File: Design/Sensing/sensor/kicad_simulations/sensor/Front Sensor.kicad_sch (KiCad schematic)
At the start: 9 parts, among them Q1 2N3904, U1 TSSP58038

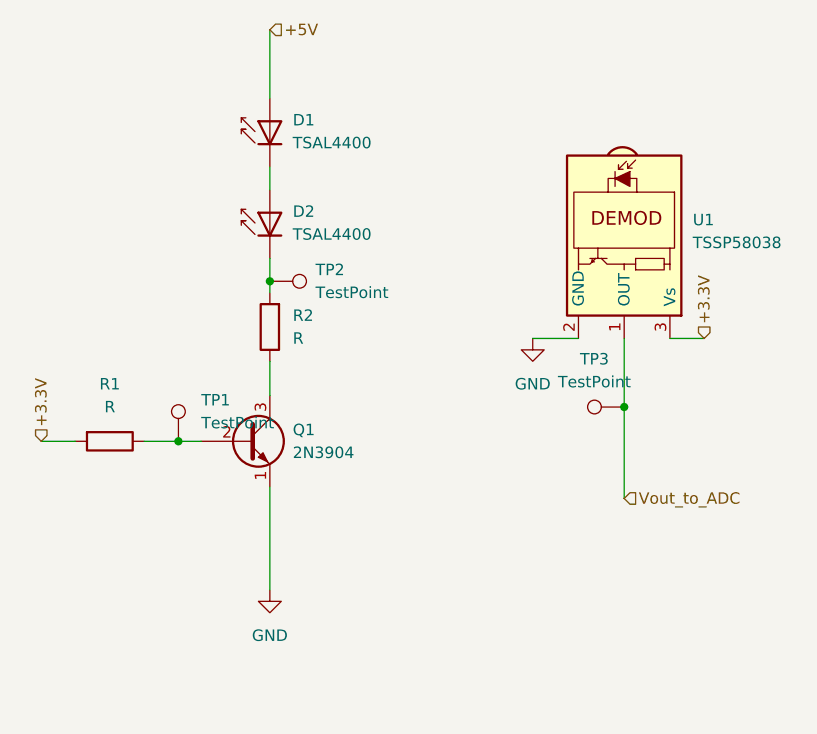
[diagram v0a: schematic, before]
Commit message: Resistor values for emitter circuit done, still have to name the circuits properly
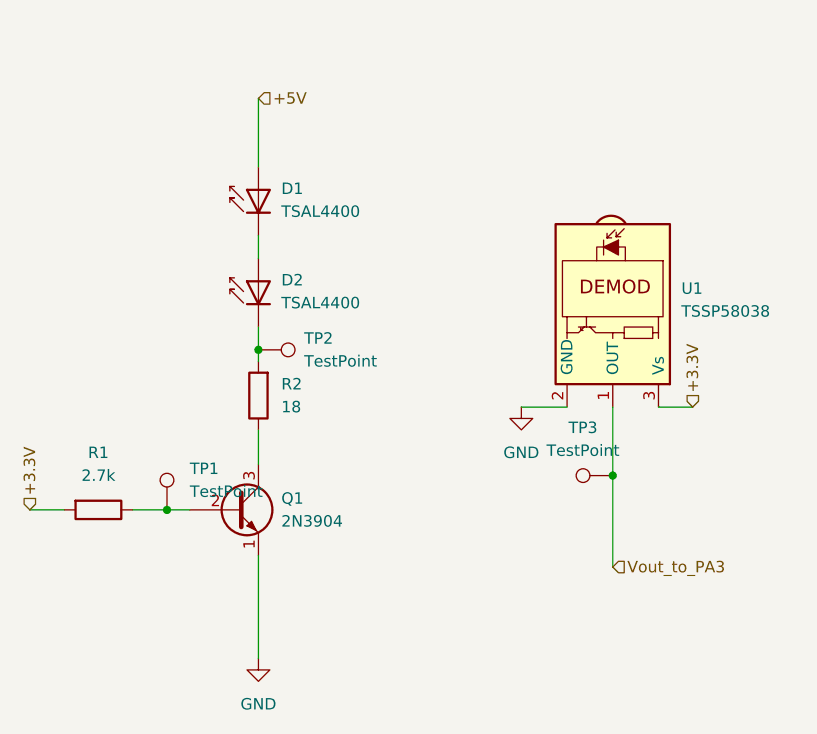
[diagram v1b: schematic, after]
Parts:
- R1: value R -> 2.7k
- R2: value R -> 18
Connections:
- net Vout_to_ADC renamed Vout_to_PA3
